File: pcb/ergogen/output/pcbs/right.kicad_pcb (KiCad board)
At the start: 2 copper layers, 143.3 x 86.2 mm, 54 parts

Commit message: Go Choc-only, add KiCad guide and case feel notes
- Drop the MX variant: one PCB per half with a Choc v1/v2 hot-swap
  footprint (center hole widened to 5.05mm for Choc v2).
- Ergogen outputs renamed to left/right PCBs and plate_left/right.
- docs/kicad-guide.md: beginner steps for finishing the PCB in KiCad.
- README: case ideas to keep a good typing feel (gasket mount,
  swappable plate materials, foam, flex cuts, weight).

Co-Authored-By: Claude Opus 5.5 <noreply@anthropic.com>
Claude-Session: https://claude.ai/code/session_017zNm7dMSTHELcztuNr6aNy
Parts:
- removed D23, D24, D25: , ComboDiode
- removed ROT1: , rotary_encoder
- removed S23, S24: , MX
- added J1: , header6, F.Cu at (209.5, -25.3)
- S1, S10, S11, S12, S13, S14, S15, S16, S17, S18, S19, S2, S20, S21, S22, S3, S4, S5, S6, S7, S8, S9: footprint MX -> Choc_V1V2_Hotswap
- moved JST1 295.3 mm to (304.8, -9.53)
- moved D19 241.1 mm to (314.3, 5.00)
- moved D20 241.1 mm to (314.3, -14.1)
- moved D3 241.1 mm to (238.1, 5.00)
- moved D4 241.1 mm to (238.1, -14.1)
- moved D7 241.1 mm to (257.2, 5.00)
- moved D8 241.1 mm to (257.2, -14.1)
- moved S19 241.1 mm to (314.3, 0.00)
- moved S20 241.1 mm to (314.3, -19.1)
- moved S3 241.1 mm to (238.1, 0.00)
- moved S4 241.1 mm to (238.1, -19.1)
- moved S7 241.1 mm to (257.2, 0.00)
- moved S8 241.1 mm to (257.2, -19.1)
- moved D11 241.1 mm to (276.2, 5.00)
- moved D12 241.1 mm to (276.2, -14.1)
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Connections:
- net left_c0_bottom renamed right_e_top
- net left_c0_home renamed right_c8_thumb
- net left_c0_thumb renamed right_e_home
- net left_c0_top renamed right_c8_bottom
- net left_c1_bottom renamed right_c8_top
- net left_c1_home renamed right_c9_thumb
- net left_c1_thumb renamed right_c8_home
- net left_c1_top renamed right_c9_bottom
- net left_c2_bottom renamed right_c9_top
- net left_c2_home renamed right_c10_thumb
- net left_c2_thumb renamed right_c9_home
- net left_c2_top renamed right_c10_bottom
- net left_c3_bottom renamed right_c10_top
- net left_c3_home renamed right_c11_thumb
- net left_c3_thumb renamed right_c10_home
- net left_c3_top renamed right_c11_bottom
- net left_c4_bottom renamed right_c11_top
- net left_c4_home renamed right_c12_thumb
- net left_c4_thumb renamed right_c11_home
- net left_c4_top renamed right_c12_bottom
- net left_c5_home renamed right_c12_top
- net left_c5_thumb renamed right_c12_home
- D1 pad 1: ROW3 -> ROW1
- D10 pad 1: ROW2 -> ROW0
- D11 pad 1: ROW1 -> ROW3
- D12 pad 1: ROW0 -> ROW2
- D13 pad 1: ROW3 -> ROW1
- D14 pad 1: ROW2 -> ROW0
- D15 pad 1: ROW1 -> ROW3
- D16 pad 1: ROW0 -> ROW2
- D17 pad 1: ROW3 -> ROW1
- D18 pad 1: ROW2 -> ROW0
- D19 pad 1: ROW1 -> ROW3
- D2 pad 1: ROW2 -> ROW0
- D20 pad 1: ROW0 -> ROW2
- D21 pad 1: ROW3 -> ROW1
- D22 pad 1: ROW1 -> ROW0
- D3 pad 1: ROW1 -> ROW3
- D4 pad 1: ROW0 -> ROW2
- D5 pad 1: ROW3 -> ROW1
- D6 pad 1: ROW2 -> ROW0
- D7 pad 1: ROW1 -> ROW3
- D8 pad 1: ROW0 -> ROW2
- D9 pad 1: ROW3 -> ROW1
- S1 pad 1: COL0 -> COL7
- S10 pad 1: COL2 -> COL9
- S11 pad 1: COL2 -> COL10
- S12 pad 1: COL2 -> COL10
- S13 pad 1: COL3 -> COL10
- S14 pad 1: COL3 -> COL10
- S15 pad 1: COL3 -> COL11
- S16 pad 1: COL3 -> COL11
- S17 pad 1: COL4 -> COL11
- S18 pad 1: COL4 -> COL11
- S19 pad 1: COL4 -> COL12
- S2 pad 1: COL0 -> COL7
- S20 pad 1: COL4 -> COL12
- S21 pad 1: COL5 -> COL12
- S22 pad 1: COL5 -> COL12
- S3 pad 1: COL0 -> COL8
- S4 pad 1: COL0 -> COL8
- S5 pad 1: COL1 -> COL8
- S6 pad 1: COL1 -> COL8
- S7 pad 1: COL1 -> COL9
- S8 pad 1: COL1 -> COL9
- S9 pad 1: COL2 -> COL9
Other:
- board size 143.3 x 86.2 mm -> 143.4 x 86.2 mm

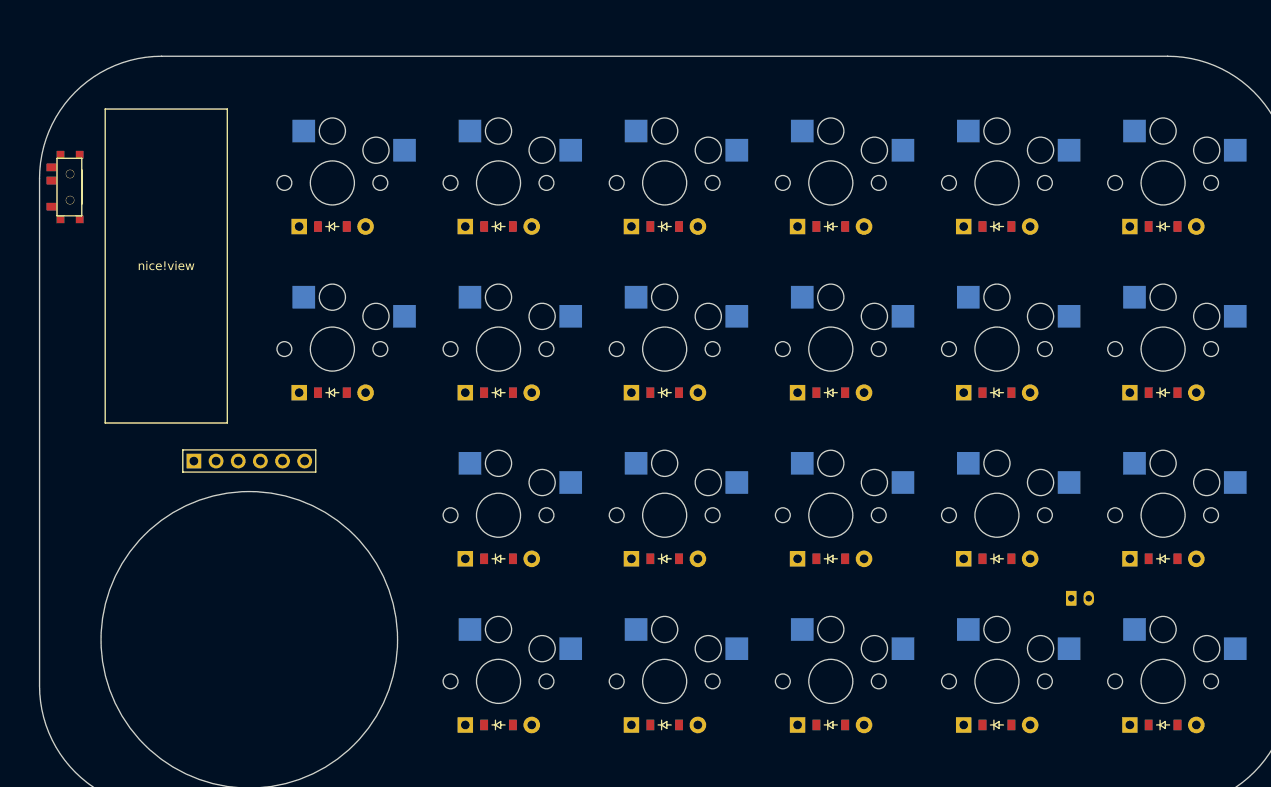
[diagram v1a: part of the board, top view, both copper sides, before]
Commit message: Use Choc v2 and ceoloide footprints for switches and peripherals
- Switches: ceoloide switch_choc_v1_v2 with v2 only (5.0mm center hole),
  hot-swap sockets on the back.
- nice!view, EC11 encoder, side power switch (Alps SSSS811101) and
  JST PH battery connector now use ceoloide footprints; nice!view is
  rotated so its pins face the XIAO and USB-C.
- Vendored footprints keep their licenses; README notes that the
  CC-BY-NC-SA parts block selling boards built from them.
- Only the XIAO nRF52840 Plus remains a placeholder.

Co-Authored-By: Claude Opus 5.5 <noreply@anthropic.com>
Claude-Session: https://claude.ai/code/session_017zNm7dMSTHELcztuNr6aNy
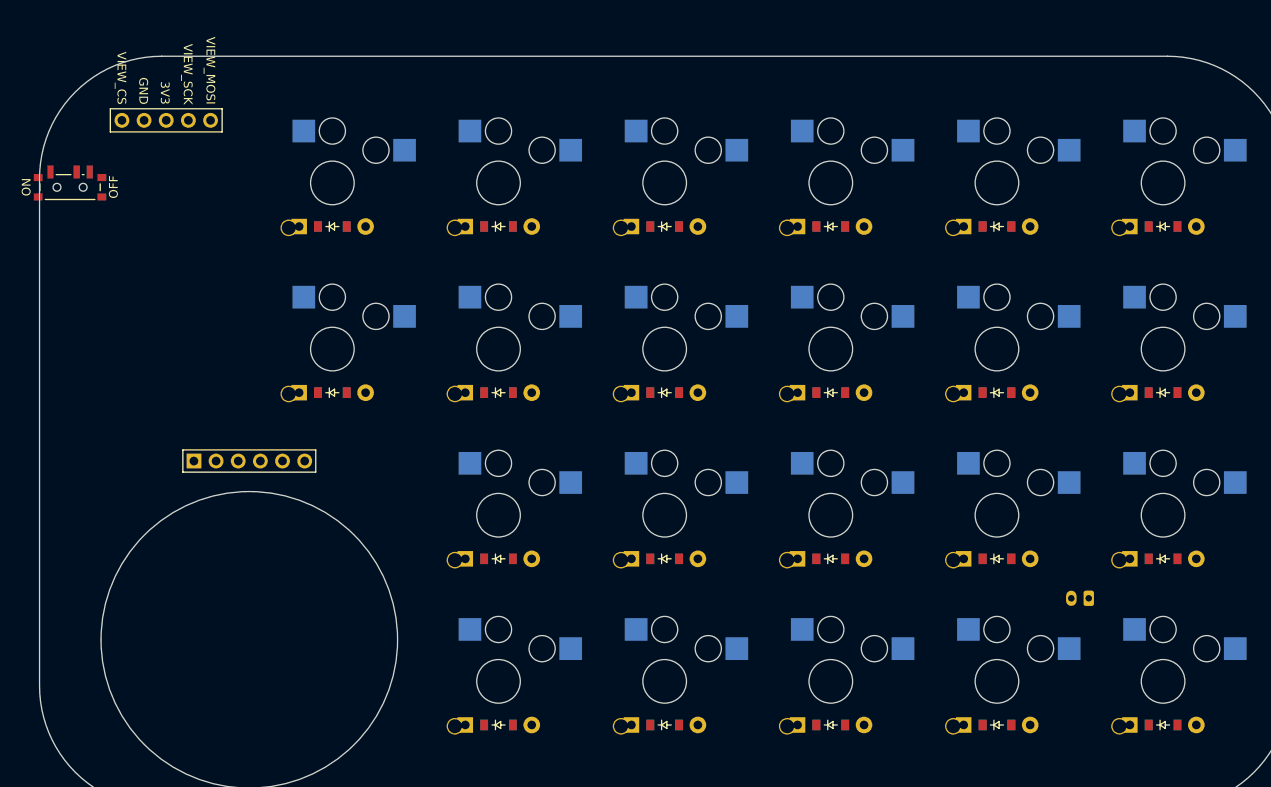
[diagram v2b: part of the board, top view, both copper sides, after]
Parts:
- removed BOX2: , box
- removed T1: , E73:SPDT_C128955
- added DISP1: , ceoloide:display_nice_view, F.Cu at (200.0, -47.6)
- added PWR1: , ceoloide:power_switch_smd_side, F.Cu at (189.0, -56.7)
- JST1: footprint JST_PH_S2B-PH-K_02x2.00mm_Angled -> ceoloide:battery_connector_jst_ph_2; moved to B.Cu
- S1, S10, S11, S12, S13, S14, S15, S16, S17, S18, S19, S2, S20, S21, S22, S3, S4, S5, S6, S7, S8, S9: footprint Choc_V1V2_Hotswap -> ceoloide:switch_choc_v1_v2; moved to B.Cu
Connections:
- JST1 pad 1: BAT_P -> GND
- JST1 pad 2: GND -> BAT_P

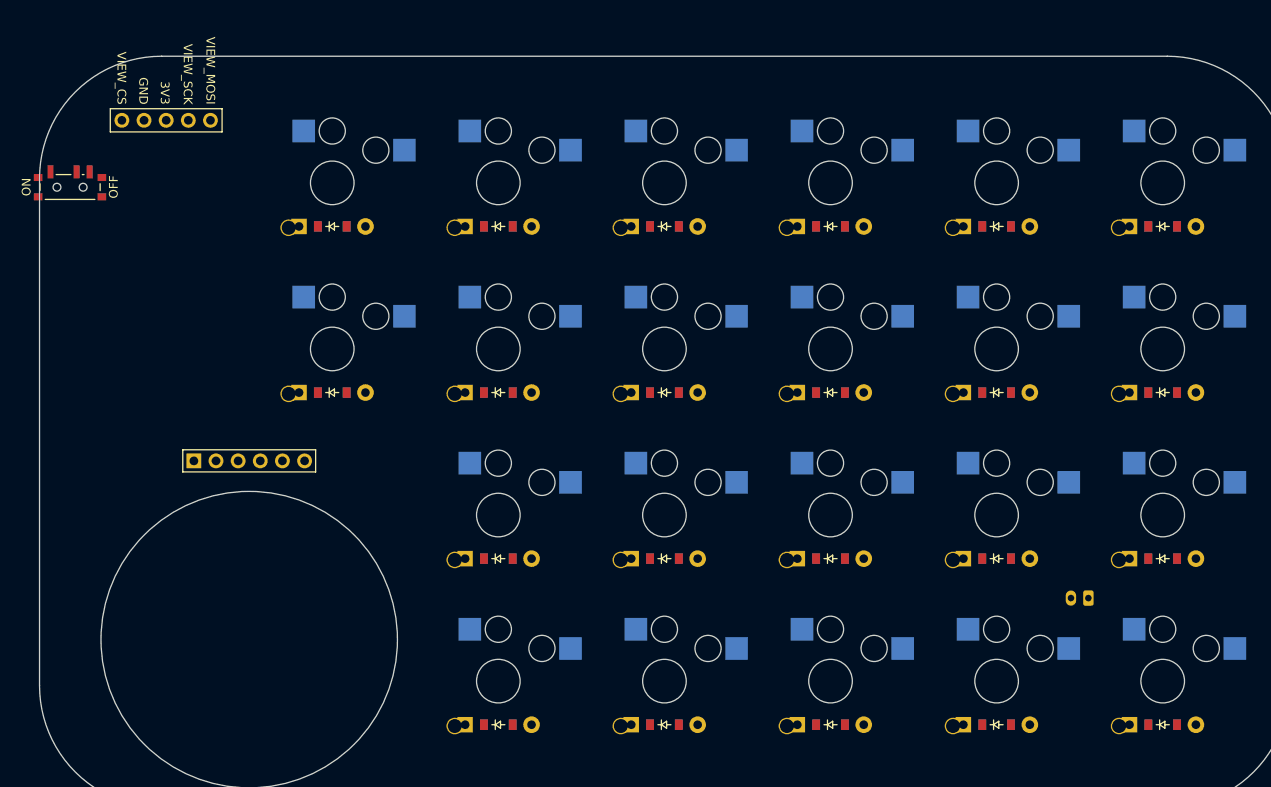
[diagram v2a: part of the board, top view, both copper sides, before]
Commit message: Replace non-commercial footprints with own ones so the PCB can be sold
- New kataware footprints: Choc v2 hot-swap (derived from Ergogen's MIT
  choc footprint, 5.0mm center hole, corner leg hole), nice!view (5 pins
  + outline), power switch placeholder (swap to KiCad SW_SPDT_PCM12) and
  an XIAO nRF52840 Plus placeholder carrying every pin's net per the
  firmware pin map.
- Keep only MIT ceoloide footprints (encoder, JST PH); drop the
  CC-BY-NC-SA ones.
- README and KiCad guide: license table and placeholder replacement.

Co-Authored-By: Claude Opus 5.5 <noreply@anthropic.com>
Claude-Session: https://claude.ai/code/session_017zNm7dMSTHELcztuNr6aNy
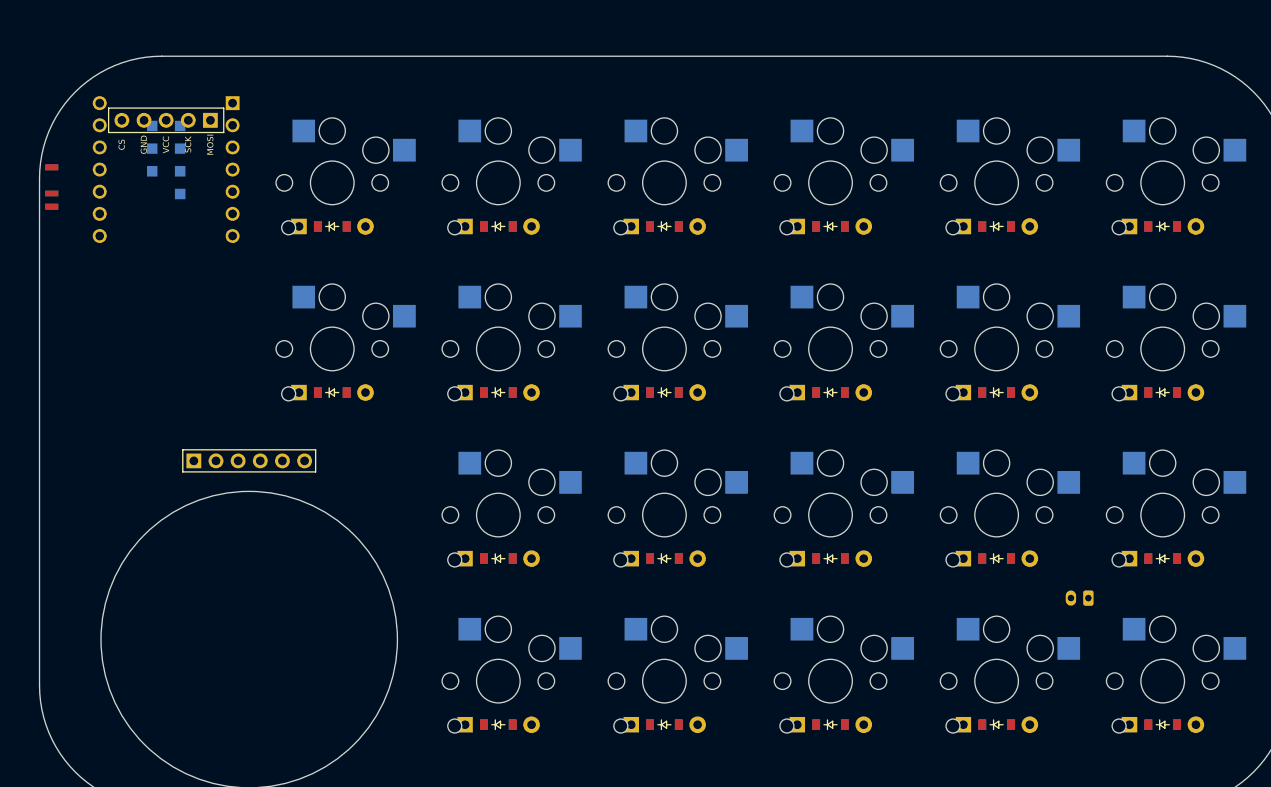
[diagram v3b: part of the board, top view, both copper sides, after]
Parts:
- removed BOX1: , box
- added MCU1: , kataware_xiao_plus_placeholder, B.Cu at (200.0, -58.7)
- DISP1: footprint ceoloide:display_nice_view -> kataware_nice_view
- PWR1: footprint ceoloide:power_switch_smd_side -> kataware_power_switch_placeholder
- S1, S10, S11, S12, S13, S14, S15, S16, S17, S18, S19, S2, S20, S21, S22, S3, S4, S5, S6, S7, S8, S9: footprint ceoloide:switch_choc_v1_v2 -> kataware_choc_v2_hotswap; moved to F.Cu

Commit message: Use a 1.25mm battery connector placeholder for the Gexa GA-011
The Gexa battery has a white 2-pin 1.25mm connector with no latch
(likely Molex PicoBlade compatible); viewed from the terminal face,
left is black (-) and right is red (+). The placeholder has pad 1 = GND
and pad 2 = BAT_P and is to be swapped for KiCad's PicoBlade footprint,
with polarity checked against the real battery.

Co-Authored-By: Claude Opus 5.5 <noreply@anthropic.com>
Claude-Session: https://claude.ai/code/session_017zNm7dMSTHELcztuNr6aNy
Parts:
- removed JST1: , ceoloide:battery_connector_jst_ph_2
- added BAT1: , kataware_battery_125_placeholder, B.Cu at (304.8, -9.53)
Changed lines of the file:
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@@
 (net 42 "BAT_SW")
 (net 43 "BAT_P")
-(net 44 "JST1_1")
-(net 45 "JST1_2")
     (module kataware_choc_v2_hotswap (layer F.Cu)
     (at 219.05 -38.1 0)
@@
     (pad 3 smd rect (at 2.25 2.1 -90) (size 0.7 1.5) (layers F.Cu F.Paste F.Mask))
     )
-    (footprint "ceoloide:battery_connector_jst_ph_2"
-        (layer "B.Cu")
-        (at 304.77500000000003 -9.525 0)
-        (property "Reference" "JST1"
-            (at 0 4.8 0)
-            (layer "B.SilkS")
-            hide
-            (effects (font (size 1 1) (thickness 0.15)))
-        )
-        (fp_line (start -2.95 -1.35) (end -2.25 -1.35) (stroke (width 0.1) (type solid)) (layer "B.Fab"))
-        (fp_line (start -2.95 6.25) (end -2.95 -1.35) (stroke (width 0.1) (type solid)) (layer "B.Fab"))
-        (fp_line (start -2.25 -1.35) (end -2.25 0.25) (stroke (width 0.1) (type solid)) (layer "B.Fab"))
-        (fp_line (start -2.25 0.25) (end 2.25 0.25) (stroke (width 0.1) (type solid)) (layer "B.Fab"))
-        (fp_line (start 2.25 -1.35) (end 2.95 -1.35) (stroke (width 0.1) (type solid)) (layer "B.Fab"))
-        (fp_line (start 2.25 0.25) (end 2.25 -1.35) (stroke (width 0.1) (type solid)) (layer "B.Fab"))
-        (fp_line (start 2.95 -1.35) (end 2.95 6.25) (stroke (width 0.1) (type solid)) (layer "B.Fab"))
-        (fp_line (start 2.95 6.25) (end -2.95 6.25) (stroke (width 0.1) (type solid)) (layer "B.Fab"))
-        (fp_line (start -3.45 -1.85) (end -3.45 10.5) (stroke (width 0.05) (type solid)) (layer "B.CrtYd"))
-        (fp_line (start -3.45 10.5) (end 3.45 10.5) (stroke (width 0.05) (type solid)) (layer "B.CrtYd"))
-        (fp_line (start 3.45 -1.85) (end -3.45 -1.85) (stroke (width 0.05) (type solid)) (layer "B.CrtYd"))
-        (fp_line (start 3.45 10.5) (end 3.45 -1.85) (stroke (width 0.05) (type solid)) (layer "B.CrtYd"))
-        (fp_line (start 1.5 7.40) (end 0.5 7.40) (stroke (width 0.1) (type solid)) (layer "B.SilkS"))
-        (fp_line (start -1.5 7.40) (end -0.5 7.40) (stroke (width 0.1) (type solid)) (layer "B.SilkS"))
-        (fp_line (start -1 6.90) (end -1 7.90) (stroke (width 0.1) (type solid)) (layer "B.SilkS"))
-        (fp_line (start -2.06 -1.46) (end -3.06 -1.46) (stroke (width 0.12) (type solid)) (layer "B.SilkS"))
-        (fp_line (start -3.06 -1.46) (end -3.06 -0.46) (stroke (width 0.12) (type solid)) (layer "B.SilkS"))
-        (fp_line (start 2.14 -1.46) (end 3.06 -1.46) (stroke (width 0.12) (type solid)) (layer "B.SilkS"))
-        (fp_line (start 3.06 -1.46) (end 3.06 -0.46) (stroke (width 0.12) (type solid)) (layer "B.SilkS"))
-        (fp_line (start -2.14 6.36) (end -3.06 6.36) (stroke (width 0.12) (type solid)) (layer "B.SilkS"))
-        (fp_line (start -3.06 6.36) (end -3.06 5.36) (stroke (width 0.12) (type solid)) (layer "B.SilkS"))
-        (fp_line (start 2.14 6.36) (end 3.06 6.36) (stroke (width 0.12) (type solid)) (layer "B.SilkS"))
-        (fp_line (start 3.06 6.36) (end 3.06 5.36) (stroke (width 0.12) (type solid)) (layer "B.SilkS"))
-        (pad "1" thru_hole roundrect (at 1 0 0) (size 1.2 1.75) (drill 0.75) (layers "*.Cu" "*.Mask") (roundrect_rratio 0.20) (net 34 "GND"))
-        (pad "2" thru_hole oval (at -1 0 0) (size 1.2 1.75) (drill 0.75) (layers "*.Cu" "*.Mask") (net 43 "BAT_P"))
+    (module kataware_battery_125_placeholder (layer B.Cu)
+    (at 304.77500000000003 -9.525 0)
+    (fp_text reference "BAT1" (at 0 -3) (layer B.SilkS) hide (effects (font (size 1 1) (thickness 0.15)) (justify mirror)))
+    (fp_text value "" (at 0 0) (layer B.SilkS) hide (effects (font (size 1 1) (thickness 0.15)) (justify mirror)))
+    (fp_text user "BAT 1.25mm (仮)" (at 0 3 0) (layer B.Fab) (effects (font (size 0.8 0.8) (thickness 0.12)) (justify mirror)))
+    (fp_text user "-" (at -0.625 -1.8 0) (layer B.SilkS) (effects (font (size 1 1) (thickness 0.15)) (justify mirror)))
+    (fp_text user "+" (at 0.625 -1.8 0) (layer B.SilkS) (effects (font (size 1 1) (thickness 0.15)) (justify mirror)))
+    (fp_line (start -2.5 -1) (end 2.5 -1) (layer B.Fab) (width 0.12))
+    (fp_line (start 2.5 -1) (end 2.5 2.2) (layer B.Fab) (width 0.12))
+    (fp_line (start 2.5 2.2) (end -2.5 2.2) (layer B.Fab) (width 0.12))
+    (fp_line (start -2.5 2.2) (end -2.5 -1) (layer B.Fab) (width 0.12))
+    (pad 1 smd rect (at -0.625 0 0) (size 0.8 1.6) (layers B.Cu B.Paste B.Mask) (net 34 "GND"))
+    (pad 2 smd rect (at 0.625 0 0) (size 0.8 1.6) (layers B.Cu B.Paste B.Mask) (net 43 "BAT_P"))
     )
   (gr_line (start 199.47500000000002 14.524999999999995) (end 314.82500000000005 14.524999999999995) (layer Edge.Cuts) (stroke (width 0.15) (type default)))
